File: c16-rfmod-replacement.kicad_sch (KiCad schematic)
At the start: 21 parts, among them J1 Conn_01x04_Pin, J2 Conn_01x04_Pin, J3 Mini-DIN-4, U1 THS7314, U2 LD1117S33TR_SOT223

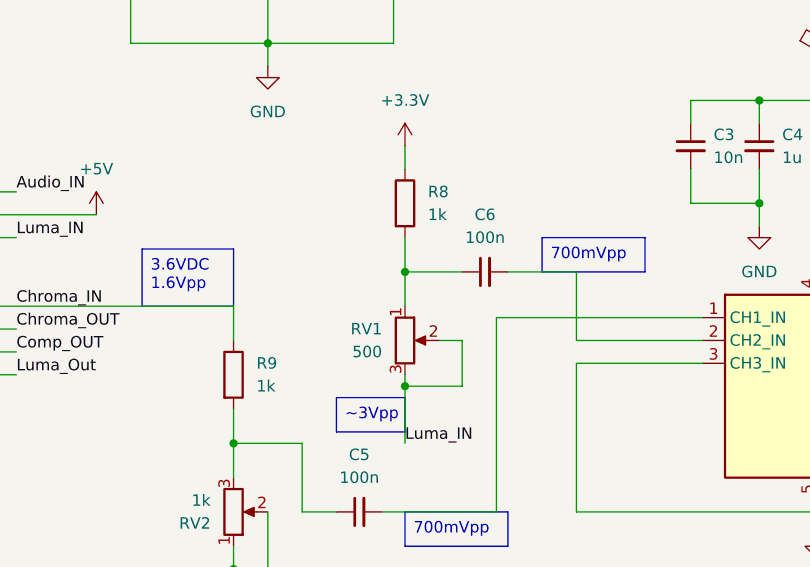
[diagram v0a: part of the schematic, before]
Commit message: Change value of R8 and RV1
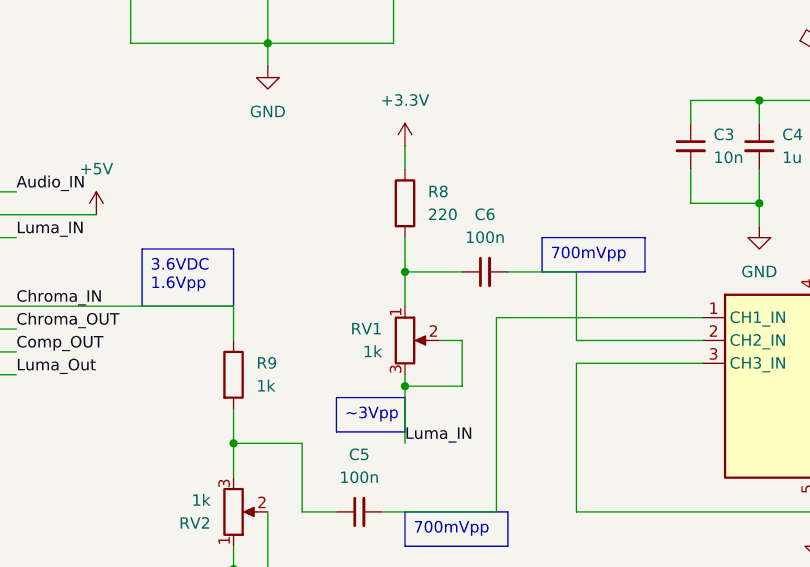
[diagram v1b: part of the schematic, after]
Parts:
- R8: value 1k -> 220
- RV1: value 500 -> 1k
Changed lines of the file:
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@@
 			)
 		)
-		(property "Value" "500"
+		(property "Value" "1k"
 			(at 76.2 81.2799 0)
 			(effects
@@
 			)
 		)
-		(property "Value" "1k"
+		(property "Value" "220"
 			(at 81.28 66.0399 0)
 			(effects

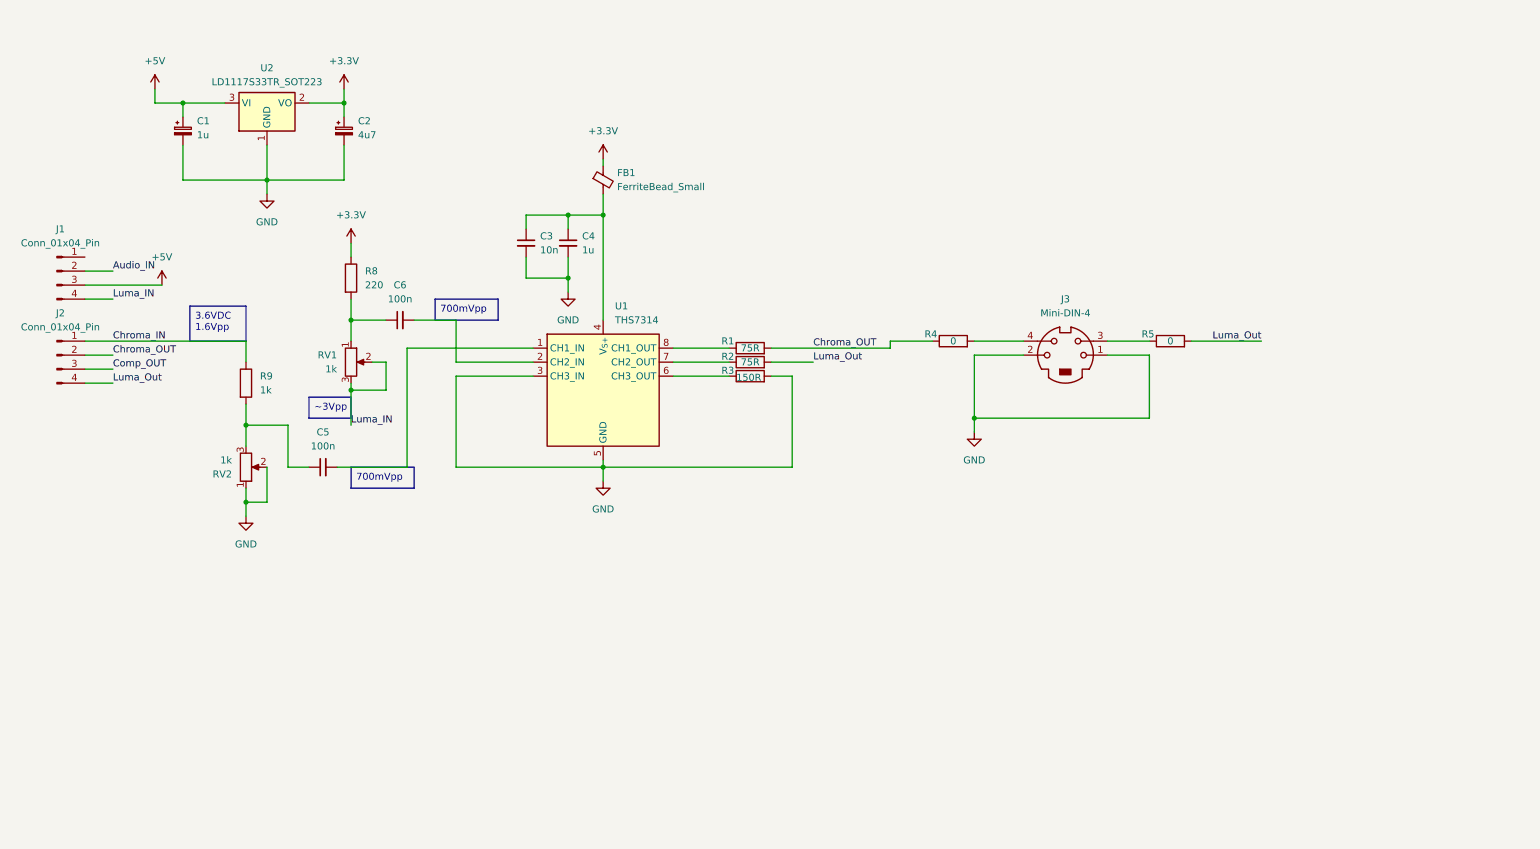
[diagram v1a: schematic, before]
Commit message: C16 RF modulator replacement Rev. B
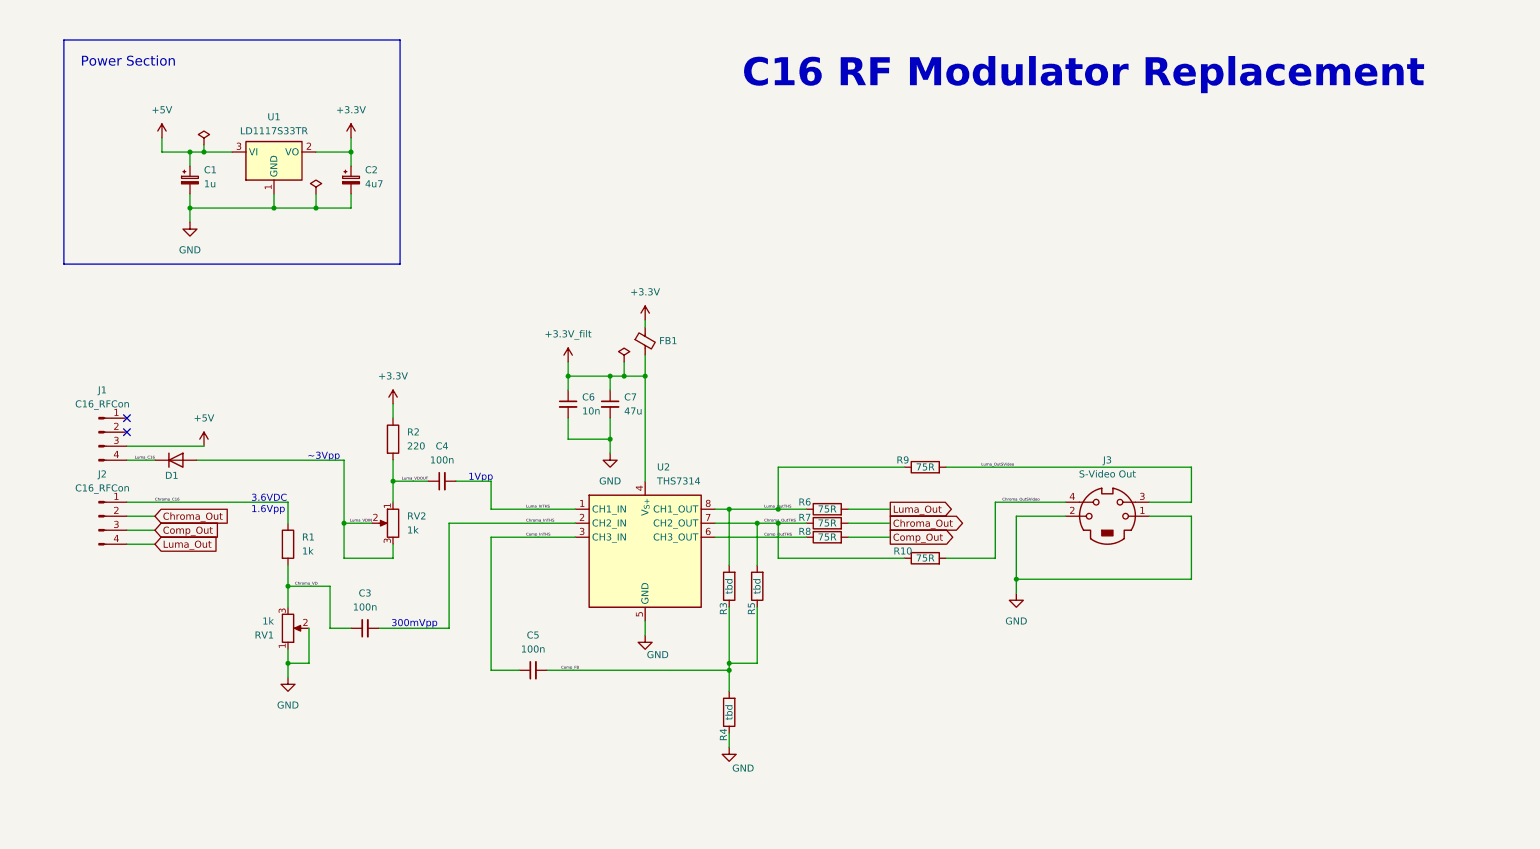
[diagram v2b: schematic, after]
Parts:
- added C5: 100n, Capacitor_SMD:C_0603_1608Metric, symbol Device:C_Small
- added D1: 1N4148WT, Diode_SMD:D_MiniMELF, symbol Diode:1N4148WT
- added R10, R8, R9: 75R, Resistor_SMD:R_0603_1608Metric, symbol Device:R
- C1: footprint Capacitor_SMD:C_0603_1608Metric_Pad1.08x0.95mm_HandSolder -> Capacitor_SMD:C_0603_1608Metric
- C2: footprint Capacitor_SMD:C_1206_3216Metric_Pad1.33x1.80mm_HandSolder -> Capacitor_SMD:C_1206_3216Metric
- C3: renamed from C5; footprint Capacitor_SMD:C_0603_1608Metric_Pad1.08x0.95mm_HandSolder -> Capacitor_SMD:C_0603_1608Metric
- C4: renamed from C6; footprint Capacitor_SMD:C_0603_1608Metric_Pad1.08x0.95mm_HandSolder -> Capacitor_SMD:C_0603_1608Metric
- C6: renamed from C3; footprint Capacitor_SMD:C_0603_1608Metric_Pad1.08x0.95mm_HandSolder -> Capacitor_SMD:C_0603_1608Metric
- C7: renamed from C4; value 1u -> 47u; footprint Capacitor_SMD:C_0603_1608Metric_Pad1.08x0.95mm_HandSolder -> Capacitor_SMD:C_1206_3216Metric
- FB1: value FerriteBead_Small -> (none); footprint Inductor_SMD:L_0603_1608Metric_Pad1.05x0.95mm_HandSolder -> Inductor_SMD:L_0603_1608Metric
- J1, J2: value Conn_01x04_Pin -> C16_RFCon
- J3: value Mini-DIN-4 -> S-Video Out
- R1: renamed from R9; footprint Resistor_SMD:R_0603_1608Metric_Pad0.98x0.95mm_HandSolder -> Resistor_SMD:R_0603_1608Metric
- R2: renamed from R8; footprint Resistor_SMD:R_0603_1608Metric_Pad0.98x0.95mm_HandSolder -> Resistor_SMD:R_0603_1608Metric
- R3: value 150R -> tbd; footprint Resistor_SMD:R_0603_1608Metric_Pad0.98x0.95mm_HandSolder -> Resistor_SMD:R_0603_1608Metric
- R4, R5: value 0 -> tbd; footprint Resistor_SMD:R_0603_1608Metric_Pad0.98x0.95mm_HandSolder -> Resistor_SMD:R_0603_1608Metric
- R6: renamed from R1; footprint Resistor_SMD:R_0603_1608Metric_Pad0.98x0.95mm_HandSolder -> Resistor_SMD:R_0603_1608Metric
- R7: renamed from R2; footprint Resistor_SMD:R_0603_1608Metric_Pad0.98x0.95mm_HandSolder -> Resistor_SMD:R_0603_1608Metric
- RV1: renamed from RV2; footprint Potentiometer_SMD:Potentiometer_Bourns_3214G_Horizontal -> Potentiometer_SMD:Potentiometer_Vishay_TS53YL_Vertical
- RV2: renamed from RV1; footprint Potentiometer_SMD:Potentiometer_Bourns_3214G_Horizontal -> Potentiometer_SMD:Potentiometer_Vishay_TS53YL_Vertical
- U1: renamed from U2; value LD1117S33TR_SOT223 -> LD1117S33TR
- renumbered U1 to U2
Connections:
- net GND: now also R4.1; no longer R3.2, U2.3 (CH3_IN)
- net Luma_Out: now also R6.2; no longer R5.2, R7.2
- net Comp_FB: now reaches R5.1
- net Comp_FB: now also R3.1, R4.2, C5.2; no longer J3.3
- net Luma_VDOUT: now reaches C4.1, R2.2, RV2.1
- net Chroma_VD: now reaches C3.1, R1.2, RV1.3
- net Chroma_InTHS: now reaches C3.2
- net Chroma_InTHS: now also U2.2 (CH2_IN); no longer U2.1 (CH1_IN)
- net Chroma_OutSVideo: now reaches J3.4
- net Chroma_OutSVideo: now also R10.2; no longer R4.2
- net Chroma_OutTHS: now reaches R7.1, U2.7 (CH2_OUT)
- net Chroma_OutTHS: now also R5.2, R10.1
- net Luma_OutTHS: now reaches R6.1, U2.8 (CH1_OUT)
- net Luma_OutTHS: now also R3.2, R9.1
- net Luma_InTHS: now reaches C4.2
- net Luma_InTHS: now also U2.1 (CH1_IN); no longer U2.2 (CH2_IN)
- net +3.3V_filt: now reaches C6.1, C7.1, FB1.2, U2.4 (V_{S+})
- net Comp_OutTHS: now reaches U2.6 (CH3_OUT)
- net Comp_OutTHS: now also R8.1; no longer R3.1
- net Audio_IN: no longer names the net of J1.2 (Pin_2)
- net Chroma_IN renamed Chroma_C16
- removed net Chroma_OUT: J2.2 (Pin_2), R4.1, R6.2
- net Comp_OUT renamed Comp_Out
- net Comp_Out: now also R8.2
- net Luma_IN renamed Luma_VDIN
- net Luma_VDIN: now also D1.2 (A); no longer J1.4 (Pin_4)
- new net Chroma_Out: J2.2 (Pin_2), R7.2
- new net Comp_InTHS: C5.1, U2.3 (CH3_IN)
- new net Luma_C16: D1.1 (K), J1.4 (Pin_4)
- new net Luma_OutSVideo: J3.3, R9.2
- no-connect marks 0 -> 2
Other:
- note added: "C16 RF Modulator Replacement"
- note added: "Power Section"
- company: (none) -> Christian Eisendle
- title: (none) -> C16 RF Modulator Replacement
- moved on the sheet: C1, C2, C3, C4, C6, C7, FB1, J1, J2, J3, R1, R2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

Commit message: Rev. C - Dual Output Amplifier
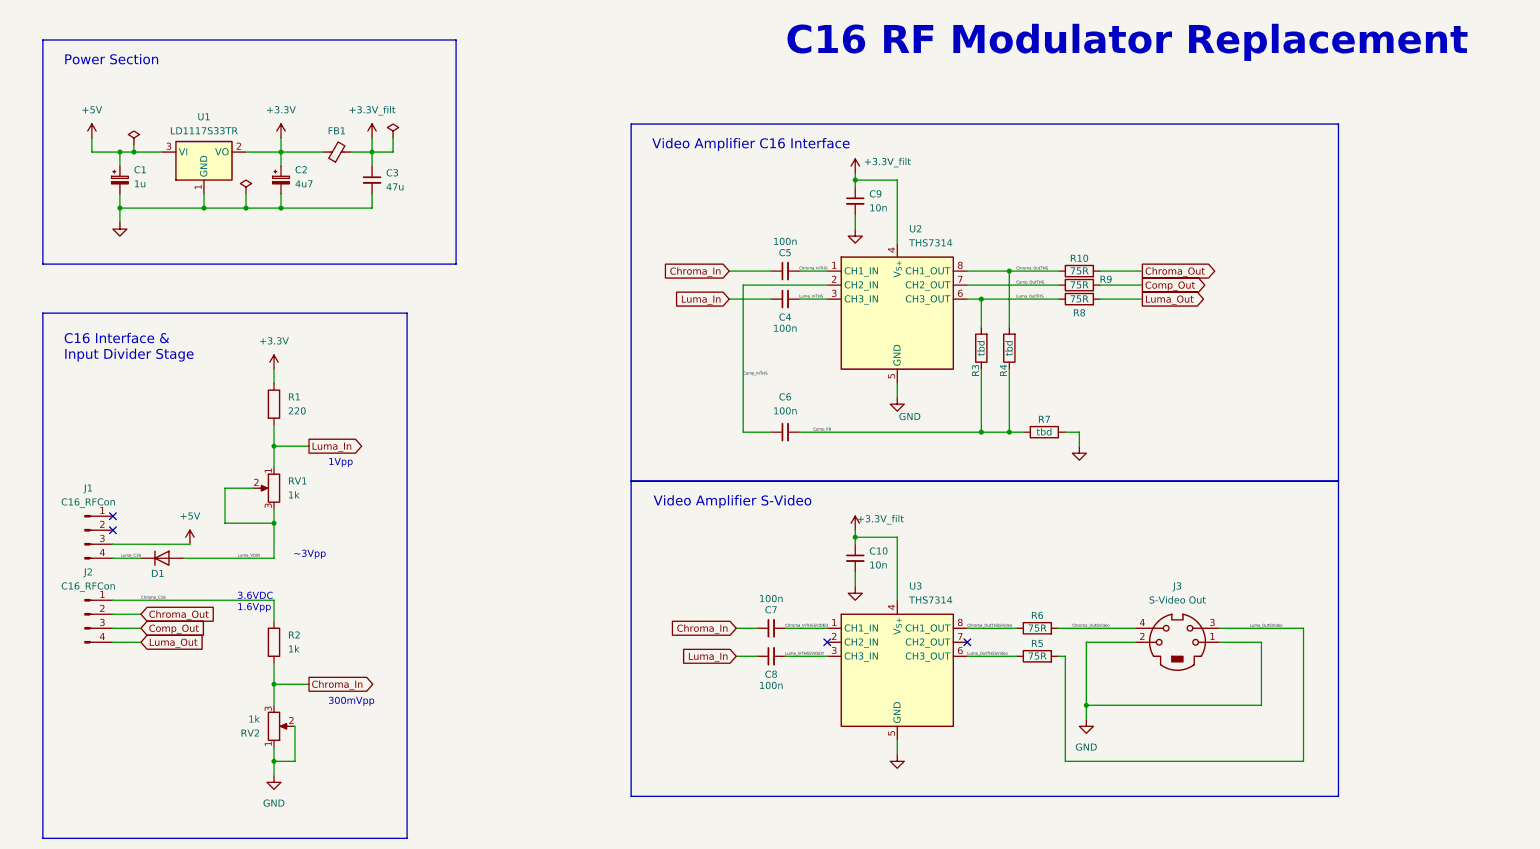
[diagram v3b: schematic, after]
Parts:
- removed C6: 10n, Capacitor_SMD:C_0603_1608Metric, symbol Device:C_Small
- removed C7: 47u, Capacitor_SMD:C_1206_3216Metric, symbol Device:C_Small
- added C10, C9: 10n, Capacitor_SMD:C_0603_1608Metric, symbol Device:C_Small
- added C3: 47u, Capacitor_SMD:C_1206_3216Metric, symbol Device:C_Small
- added C4, C5: 100n, Capacitor_SMD:C_0603_1608Metric, symbol Device:C_Small
- added U3: THS7314, Package_SO:SOIC-8_3.9x4.9mm_P1.27mm, symbol c16-rfmod-replacement:THS7315
- renumbered C5 to C6, C3 to C7, C4 to C8, R2 to R1, R7 to R10, R1 to R2, R5 to R4, R9 to R5, R10 to R6, R4 to R7, R6 to R8, R8 to R9, RV2 to RV1, RV1 to RV2
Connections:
- net +3.3V_filt: now also C10.1, C3.1, C9.1, U3.4 (V_{S+})
- net Chroma_InTHS: now also U2.1 (CH1_IN), C5.2; no longer C7.2, U2.2 (CH2_IN)
- net Chroma_OutTHS: now also U2.8 (CH1_OUT); no longer R6.1, U2.7 (CH2_OUT)
- net Comp_InTHS: now also U2.2 (CH2_IN); no longer U2.3 (CH3_IN)
- net Comp_OutTHS: now also U2.7 (CH2_OUT); no longer U2.6 (CH3_OUT)
- net GND: now also C10.2, C3.2, C9.2, U3.5 (GND)
- net Luma_InTHS: now also U2.3 (CH3_IN), C4.2; no longer C8.2, U2.1 (CH1_IN)
- net Luma_OutTHS: now also U2.6 (CH3_OUT); no longer R5.1, U2.8 (CH1_OUT)
- net Chroma_VD renamed Chroma_In
- net Chroma_In: now also C5.1
- net Luma_VDOUT renamed Luma_In
- net Luma_In: now also C4.1
- new net Chroma_InTHSSVIDEO: C7.2, U3.1 (CH1_IN)
- new net Chroma_OutTHSSVideo: R6.1, U3.8 (CH1_OUT)
- new net Luma_InTHSSVIDEO: C8.2, U3.3 (CH3_IN)
- new net Luma_OutTHSSVideo: R5.1, U3.6 (CH3_OUT)
- no-connect marks 2 -> 4
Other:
- note added: "C16 Interface & Input Divider Stage"
- note added: "Video Amplifier C16 Interface"
- note added: "Video Amplifier S-Video"
- moved on the sheet: C1, C2, C6, C7, C8, D1, J1, J2, J3, R1, R10, R2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
